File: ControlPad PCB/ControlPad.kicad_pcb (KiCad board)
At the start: 2 copper layers, 19 parts, among them SW1 SW_Push, SW10 SW_Push, SW2 SW_Push, SW3 SW_Push, SW4 SW_Push, SW6 SW_Push, SW7 SW_Push, SW8 SW_Push, SW9 SW_Push, U1 MOUDLE-SEEEDUINO-XIAO

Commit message: Traces Routing V1
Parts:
- moved D9 68.6 mm to (186.7, 104.8)
- moved D8 62.3 mm to (167.6, 104.8)
- moved D7 61.7 mm to (148.6, 104.8)
- moved D6 54.5 mm to (177.2, 85.7)
- moved D3 46.9 mm to (167.6, 66.7)
- moved U1 45.2 mm to (112.3, 56.5), turned to 180 degrees
- moved D5 43.8 mm to (158.1, 85.7)
- moved SW3 42.6 mm to (174.0, 52.1)
- moved SW8 42.6 mm to (154.9, 90.2)
- moved D4 40.3 mm to (139.1, 85.7)
- moved D2 30.5 mm to (148.6, 66.7)
- moved SW2 21.3 mm to (154.9, 52.1)
- moved SW4 21.3 mm to (145.4, 71.1)
- moved SW7 21.3 mm to (183.5, 71.1)
- moved SW9 21.3 mm to (174.0, 90.2)
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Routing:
- net Net-(D7-K): track 0.00 -> 114.3 mm
- net Net-(U1-PA9_A5_D5_SCL): track 0.00 -> 107.3 mm
- net Net-(D4-K): track 0.00 -> 91.5 mm
- net Net-(U1-PB08_A6_D6_TX): track 0.00 -> 90.2 mm
- net Net-(U1-PB09_A7_D7_RX): track 0.00 -> 81.1 mm
- net Net-(D1-K): track 0.00 -> 69.8 mm
- net Net-(D2-A): track 0.00 -> 15.2 mm
- net Net-(D9-A): track 0.00 -> 15.1 mm
- net Net-(D7-A): track 0.00 -> 15.1 mm
- net Net-(D6-A): track 0.00 -> 15.1 mm
- net Net-(D5-A): track 0.00 -> 15.1 mm
- net Net-(D4-A): track 0.00 -> 15.1 mm
- net Net-(D8-A): track 0.00 -> 15.1 mm
- net Net-(D1-A): track 0.00 -> 15.1 mm
- net Net-(D3-A): track 0.00 -> 15.1 mm

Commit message: Traces Routing V2
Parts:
- moved U1 1.58 mm to (113.8, 56.4)
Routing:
- net Net-(U1-PB08_A6_D6_TX): track 90.2 -> 88.0 mm
- net Net-(D4-K): track 91.5 -> 90.0 mm
- net Net-(D1-K): track 69.8 -> 68.2 mm
- net Net-(U1-PA9_A5_D5_SCL): track 107.3 -> 105.9 mm
- net Net-(D7-K): track 114.3 -> 112.9 mm
- net Net-(U1-PB09_A7_D7_RX): track 81.1 -> 80.3 mm
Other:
- board outline added: 98.4 x 62.6 mm

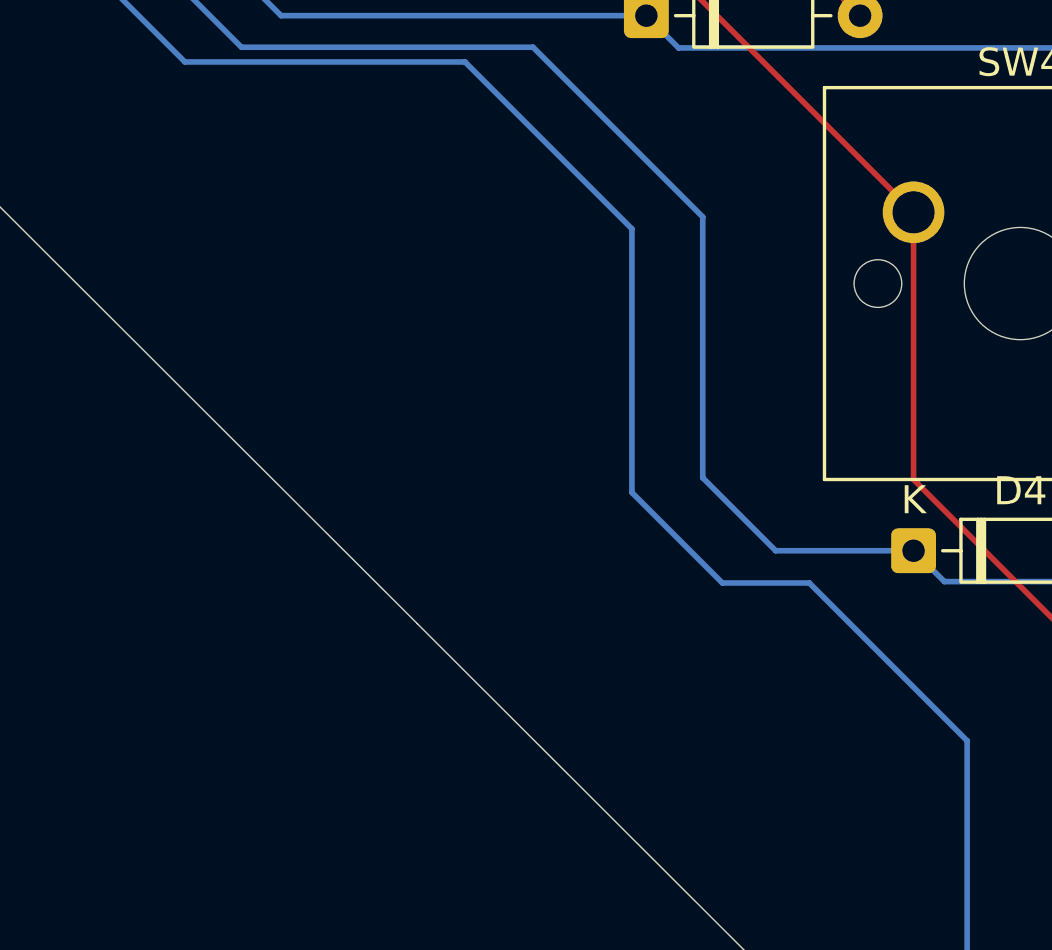
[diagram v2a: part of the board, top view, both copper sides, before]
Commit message: Silk Screen Art and PCB Boader
I added a ControlPad Logo and Hack Club logo to the silkscreen of the PCB and I added a boarder.
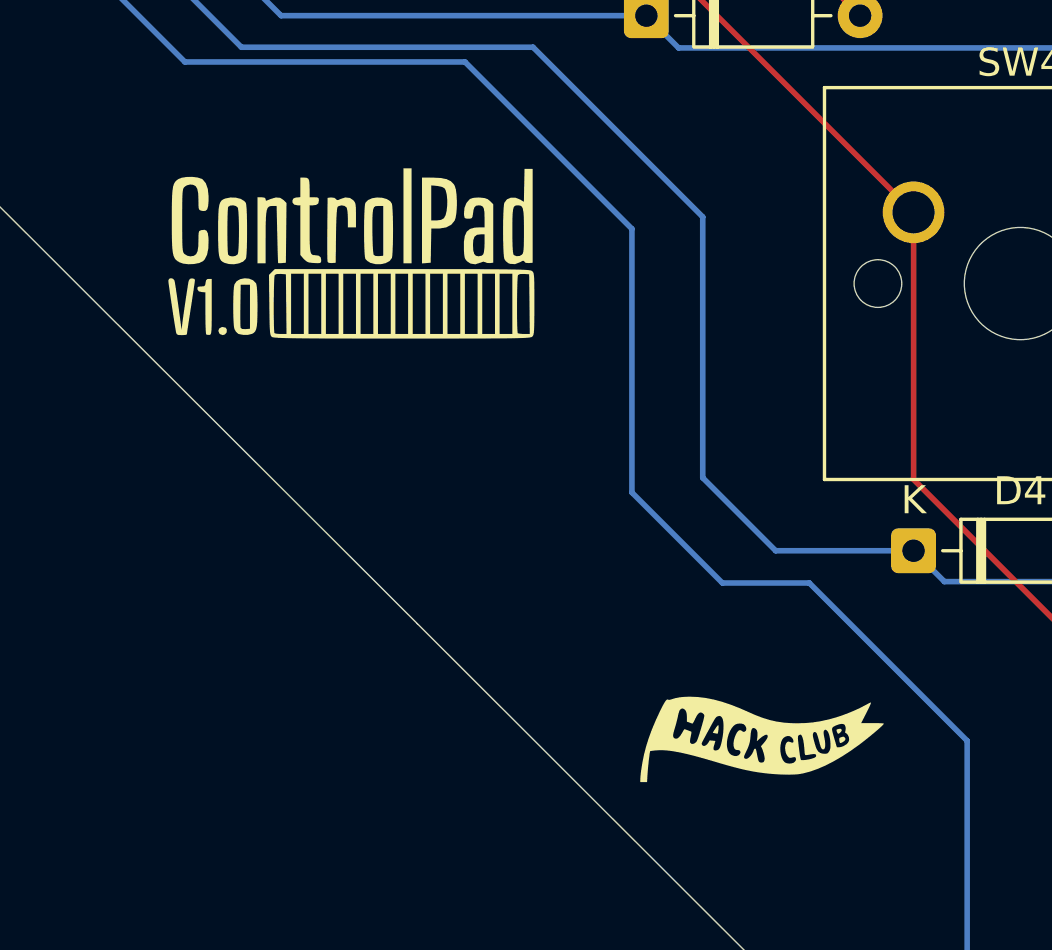
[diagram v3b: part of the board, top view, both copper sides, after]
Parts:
- added G***: LOGO, Silkscreen Art footprints:ControlPad Silkscreen Art Footprint 2, F.Cu at (166.8, 73.1)
- added G***: LOGO, Silkscreen Art footprints:Hack Club Art, F.Cu at (133.7, 92.5)
